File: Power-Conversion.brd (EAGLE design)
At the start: 218.4 x 101.6 mm, 48 parts, among them Q1 SUM90P10-19L, U7 LM2678

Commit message: Shrinking down the board more and figuring out part placement
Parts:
- removed J3, J4: (no value), SparkFun-Connectors:BANANA_CONN
- added U$13, U$14: POWER_BRICK_CONNECTORS(2X15), MotherBoardParts2:POWER_BRICK_CONNECTORS(2X15)
- moved R15 215.0 mm to (225.0, 63.8)
- moved J1 208.7 mm to (212.1, 36.6)
- moved J2 208.6 mm to (212.1, 45.7)
- moved R5 207.6 mm to (219.7, 65.0)
- moved U$7 204.7 mm to (227.1, 55.4)
- moved U$5 202.7 mm to (226.6, 71.6)
- moved D1 200.3 mm to (229.1, 26.9)
- moved R3 199.7 mm to (229.4, 21.6), turned to 90 degrees
- moved Q1 198.8 mm to (216.4, 26.9)
- moved C2 196.4 mm to (232.4, 40.6)
- moved R4 196.4 mm to (232.4, 38.6)
- moved U$1 196.3 mm to (234.9, 32.3)
- moved C1 195.0 mm to (229.4, 35.1)
- moved U$16 148.3 mm to (143.8, 148.6)
- moved U$8 134.7 mm to (152.8, 132.2)
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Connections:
- net +48V: no longer J4.P$1
- net +48V_RAW: no longer J3.P$1
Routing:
- net GND: track 0.87 -> 0.00 mm
- net +5V: track 0.83 -> 0.00 mm
- removed copper zone on layer 1, net +48V
- removed copper zone on layer 1, net +48V_RAW
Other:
- board size 218.4 x 101.6 mm -> 182.9 x 101.6 mm

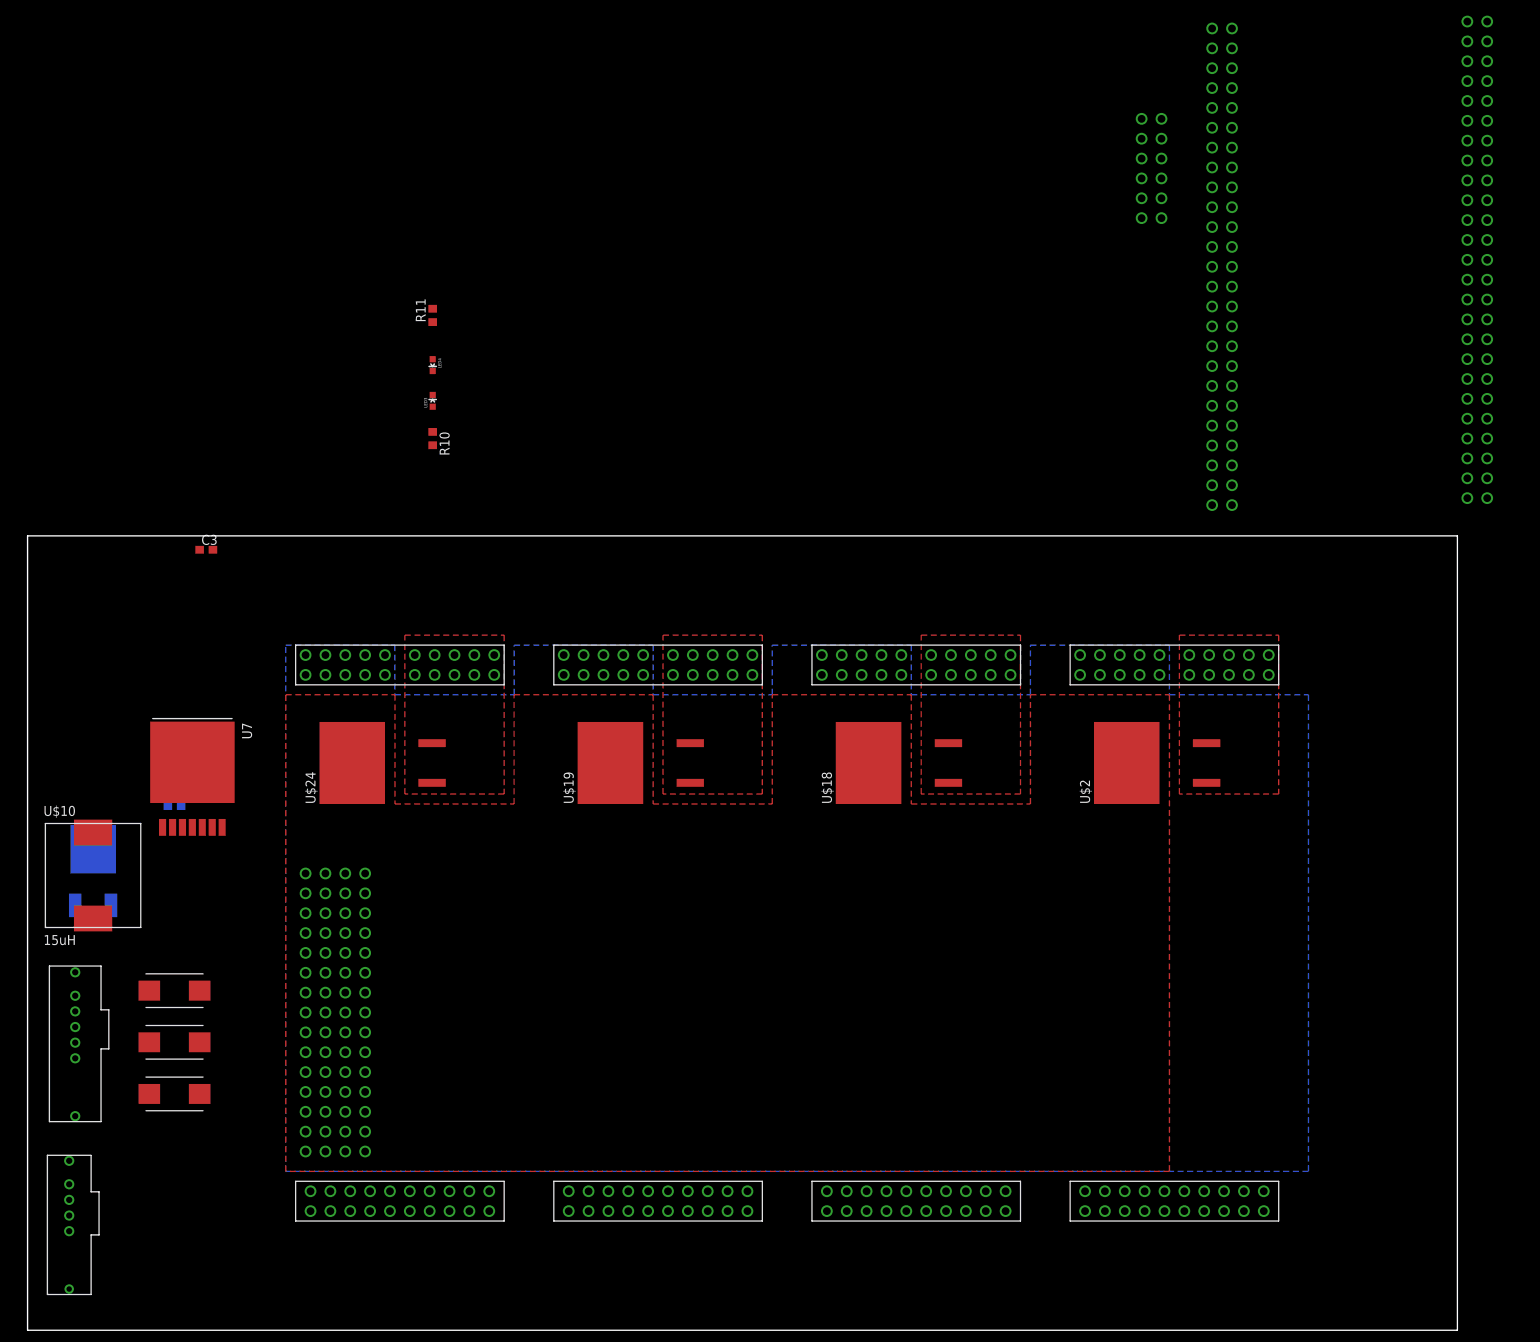
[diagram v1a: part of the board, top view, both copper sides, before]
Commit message: Finalizing intial layout of parts
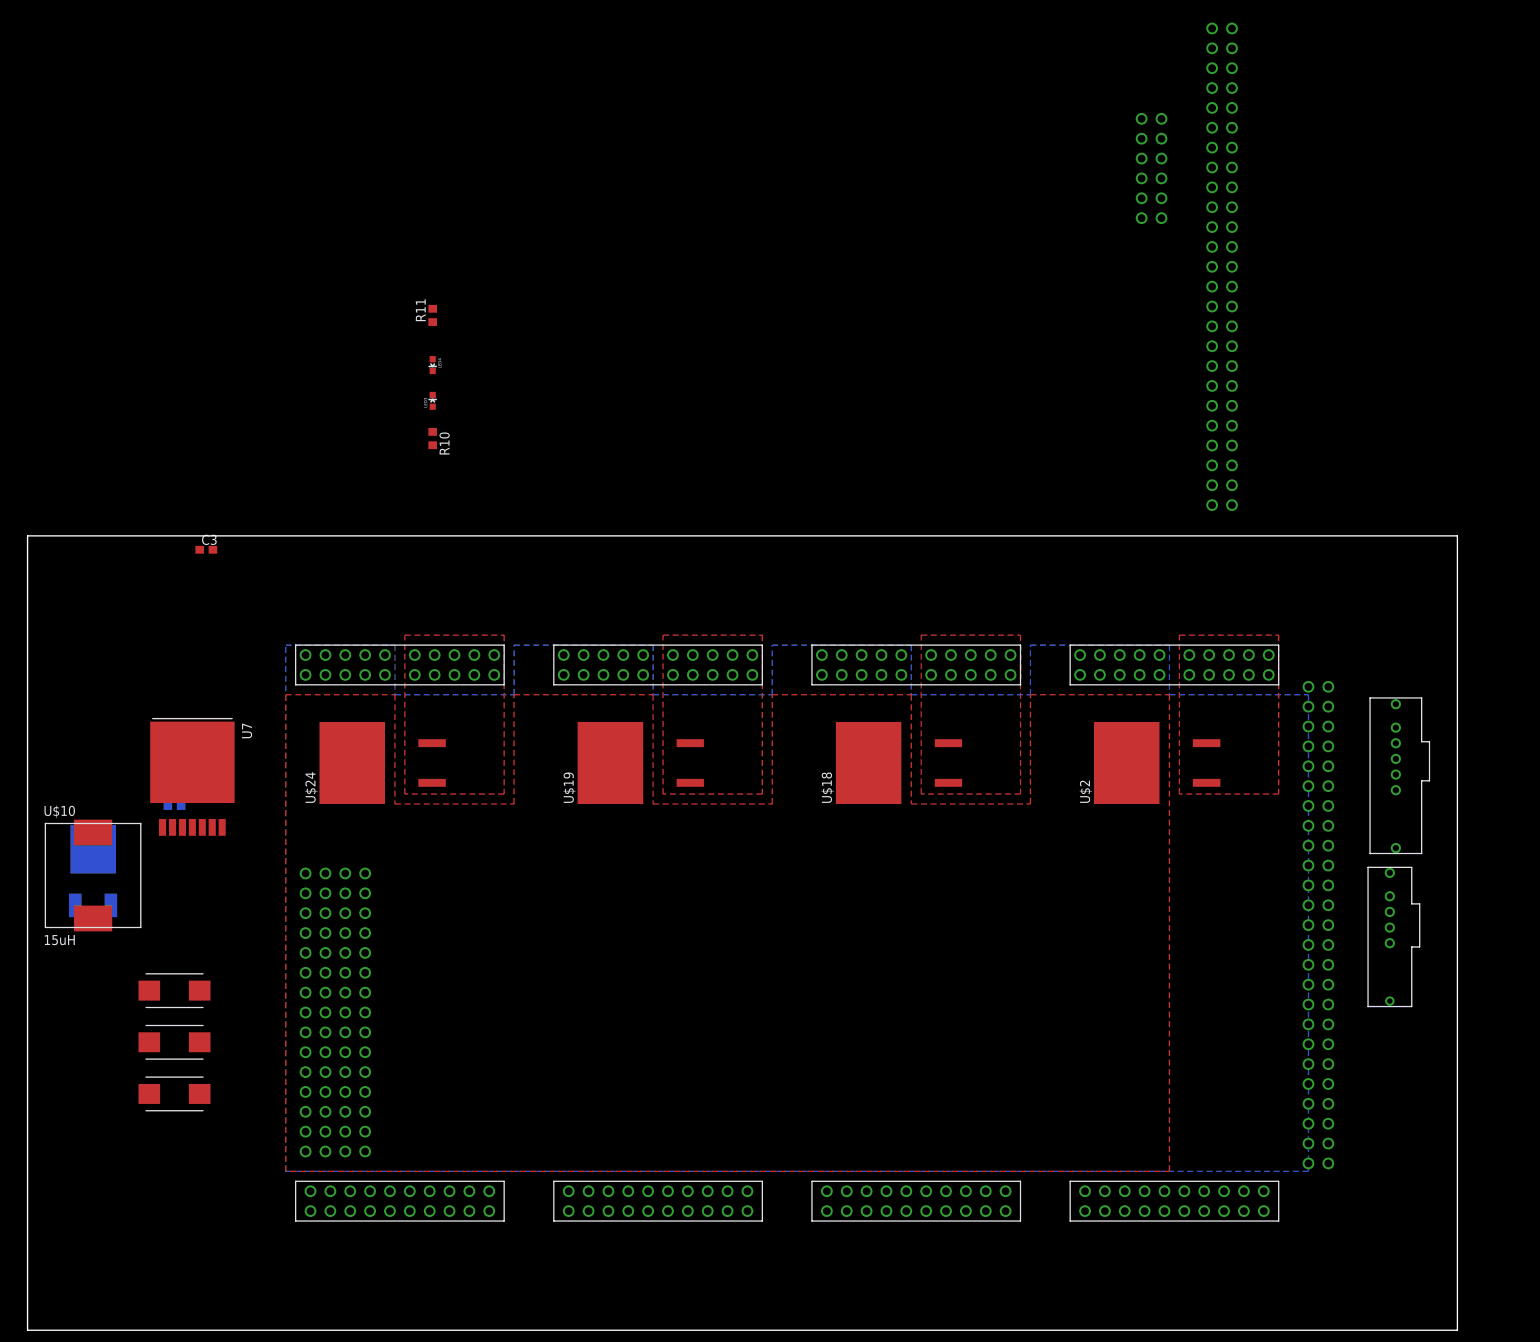
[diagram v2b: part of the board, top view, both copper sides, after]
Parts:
- moved U$12 172.9 mm to (177.0, 41.4)
- moved U$11 172.4 mm to (178.3, 80.8)
- moved U$3 80.1 mm to (165.1, 55.6), turned to 0 degrees

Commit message: Moved around parts to near final postions.  Next comes routing.
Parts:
- added U$15: POWER_DIST_TO_ESC, MotherBoardParts2:POWER_DIST_TO_ESC
- moved R15 210.0 mm to (22.4, 8.89), turned to 180 degrees
- moved R5 205.8 mm to (22.4, 6.86), turned to 0 degrees
- moved U$11 191.5 mm to (3.30, 3.05), turned to 270 degrees
- moved U$12 164.9 mm to (13.5, 20.8), turned to 270 degrees
- moved U$16 142.4 mm to (13.7, 90.7), turned to 90 degrees
- moved R11 109.2 mm to (6.35, 30.5)
- moved LED3 105.0 mm to (3.56, 25.7)
- moved LED4 105.0 mm to (3.56, 30.2)
- moved R10 98.5 mm to (6.35, 26.7)
- moved U$1 85.9 mm to (150.6, 15.7), flipped to the bottom, turned to 90 degrees
- moved R3 83.4 mm to (148.1, 3.05), flipped to the bottom
- moved D1 83.2 mm to (148.1, 7.87), flipped to the bottom
- moved U$6 81.6 mm to (163.3, 19.8), turned to 180 degrees
- moved R2 81.2 mm to (160.3, 19.6), turned to 270 degrees
- moved C2 79.4 mm to (157.2, 15.2), flipped to the bottom
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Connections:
- removed net +48V_SNS: U$1.3, U$1.4
- net VCC: now also U$1.3, U$1.4
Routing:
- net GND: track 0.00 -> 8.33 mm
- net N$25: track 0.00 -> 4.51 mm, vias 0 -> 1
- net N$36: track 0.00 -> 4.51 mm, vias 0 -> 1
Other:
- board size 182.9 x 101.6 mm -> 182.9 x 114.3 mm

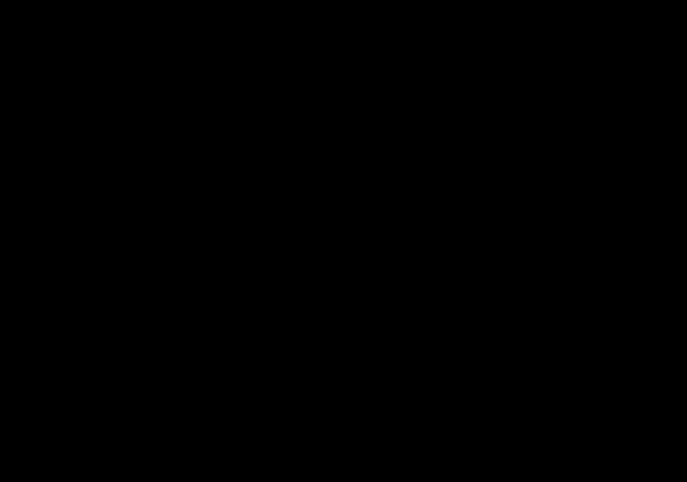
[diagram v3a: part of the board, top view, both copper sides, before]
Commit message: Added fuse to 12V going to rasp pi
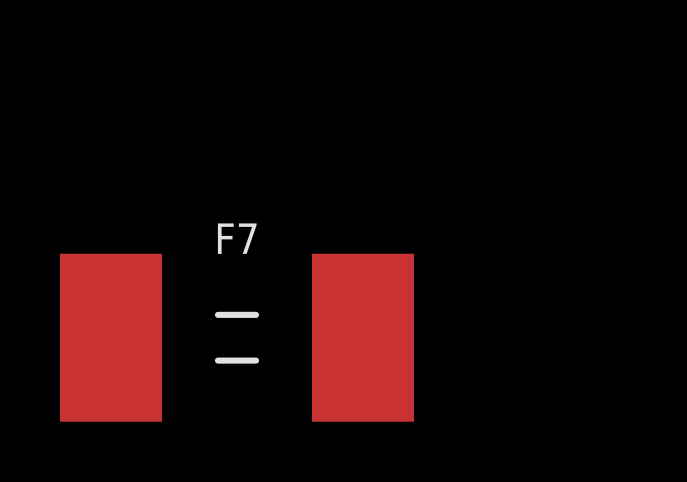
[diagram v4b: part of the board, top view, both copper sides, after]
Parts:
- added F7: 10A, PowerComponents:PTC-2920
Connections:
- new net N$1: C11.+, C12.+, C13.+, C14.+, C3.1, F7.1, U7.2
- net +12V: now also F7.2; no longer C11.+, C12.+, C13.+, C14.+, C3.1, U7.2

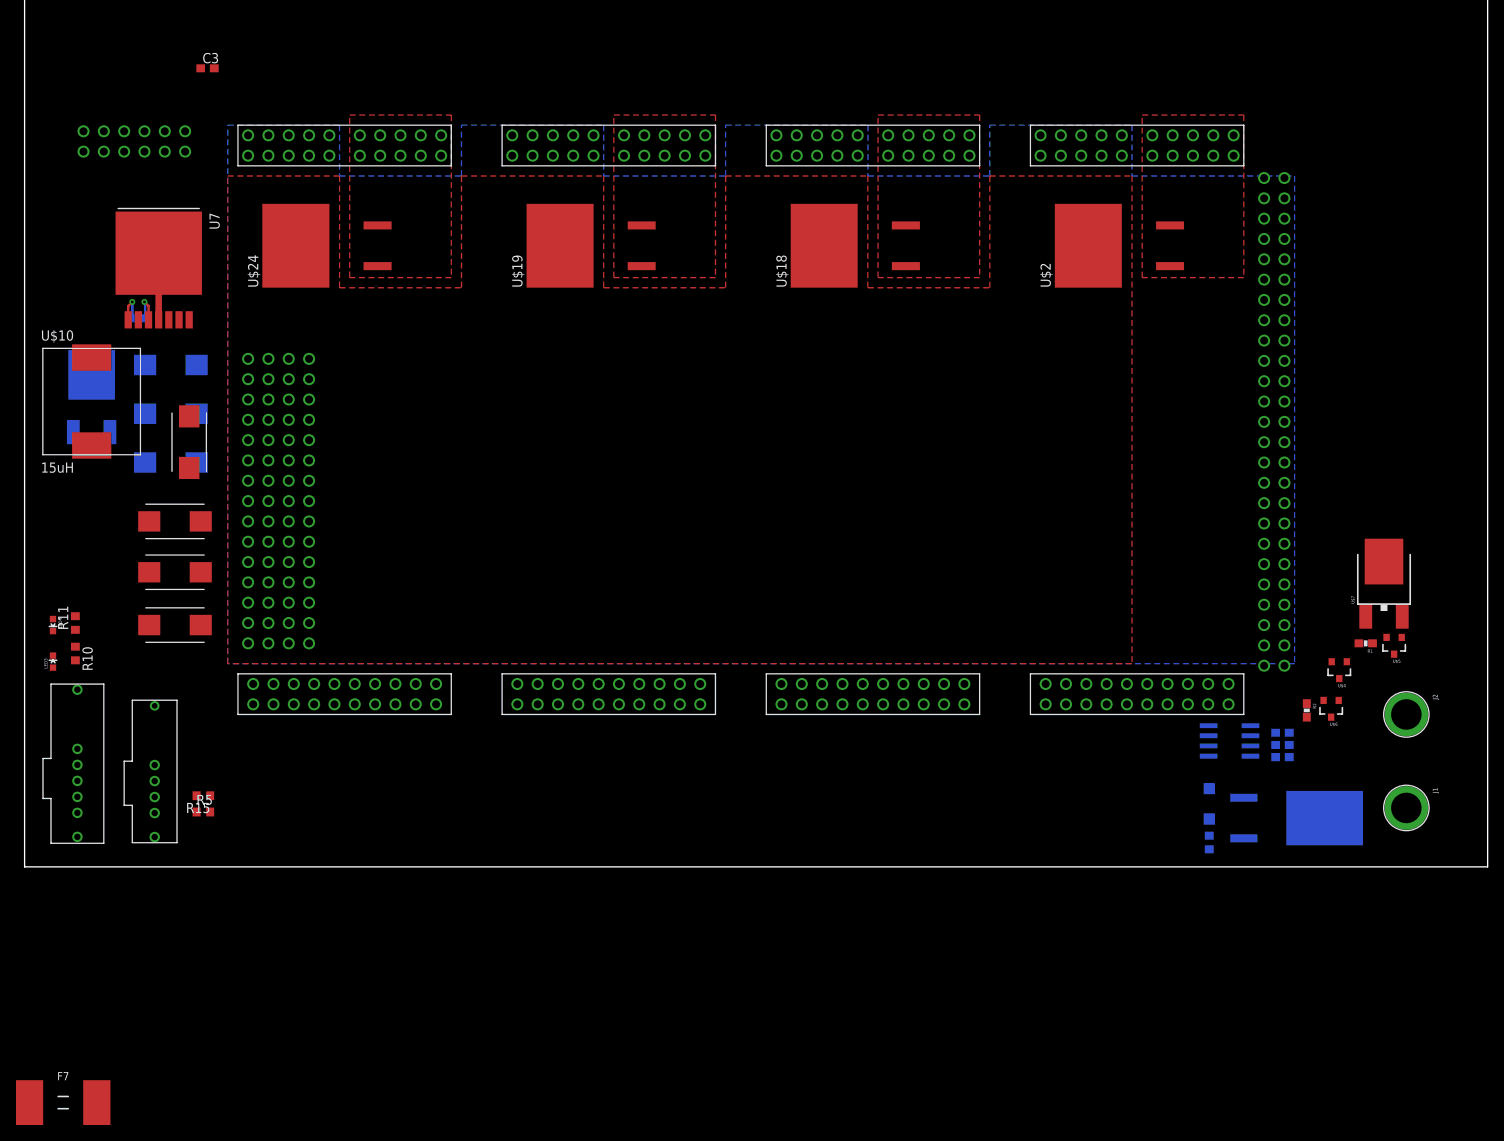
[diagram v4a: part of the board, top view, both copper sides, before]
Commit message: Got buck regulator done
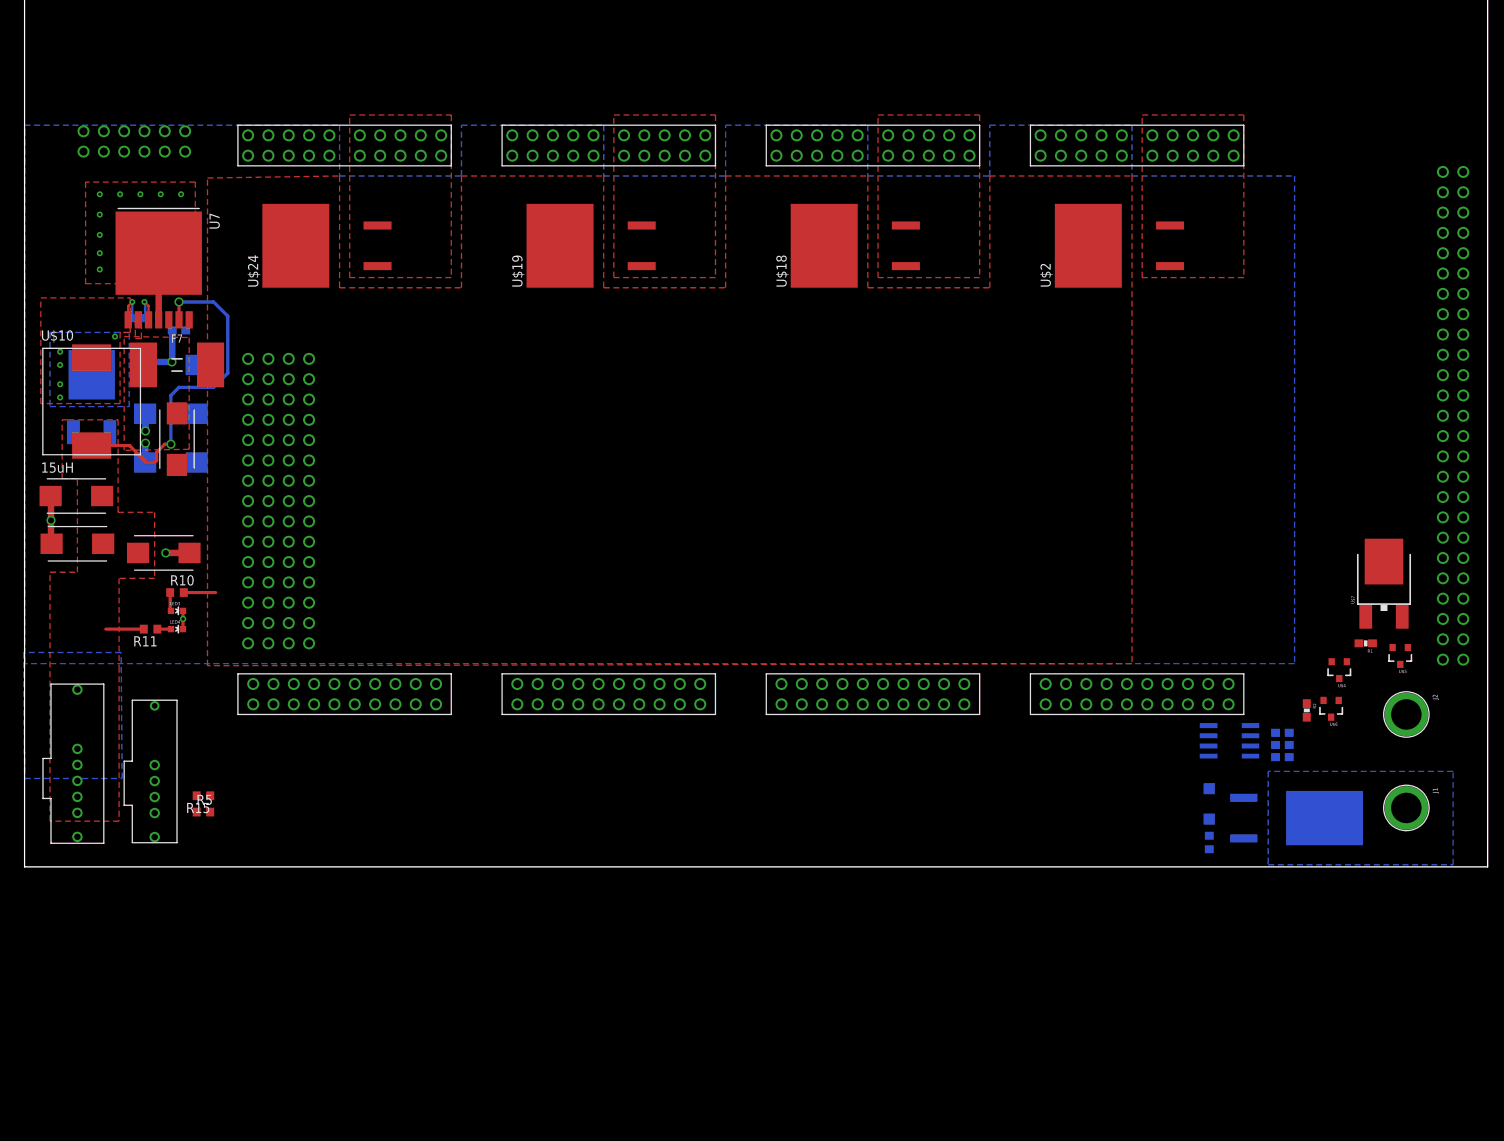
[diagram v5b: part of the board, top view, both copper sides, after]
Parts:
- moved F7 93.3 mm to (19.1, 62.7)
- moved C3 33.0 mm to (19.3, 67.1), flipped to the bottom, turned to 180 degrees
- moved U$3 22.4 mm to (178.6, 60.2)
- moved C9 20.3 mm to (6.48, 46.4), turned to 180 degrees
- moved LED3 16.7 mm to (19.1, 32.0), turned to 270 degrees
- moved LED4 15.5 mm to (19.1, 29.7), turned to 270 degrees
- moved R10 14.8 mm to (19.1, 34.3), turned to 0 degrees
- moved C10 12.7 mm to (6.60, 40.4), turned to 180 degrees
- moved R11 9.43 mm to (15.7, 29.7), turned to 180 degrees
- moved C8 4.18 mm to (17.4, 39.2)
- moved C14 1.57 mm to (19.1, 53.5)
- moved U$5 1.48 mm to (172.0, 26.4)
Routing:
- net +5V: track 0.00 -> 47.6 mm, vias 0 -> 2
- net N$1: track 0.00 -> 12.4 mm, vias 0 -> 3
- net GND: track 8.33 -> 19.7 mm, vias 0 -> 12
- net +12V: track 0.00 -> 3.98 mm
- net N$39: track 0.00 -> 2.33 mm
- net N$40: track 0.00 -> 1.70 mm
- net N$36: vias 1 -> 6
- added copper zone on layer 16, net +48V_RAW
- added copper zone on layer 1, net +5V
- added copper zone on layer 1, net GND
- added copper zone on layer 1, net N$1
- added copper zone on layer 1, net N$36
- added copper zone on layer 16, net N$36
